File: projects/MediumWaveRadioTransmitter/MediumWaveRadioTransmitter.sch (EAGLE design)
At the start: 20 parts, among them P4 100k, Q1 400kH, T1 BC337, T2 BC337

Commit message: fix: mwrt fixed a little bit
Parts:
- removed 12V, GND, TP1, TP2, TP3: SE13, solpad:SE13
- added X1: IN_OUT, con-wago-508:W237-05P
- T1, T2: device transistor:BC337 -> transistor:BC337-16-NPN-TO92-CBE
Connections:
- removed net N$4: C1.2, C2.2, C3.2, GND.MP, P4.A, Q1.2, R8.1, R9.1
- new net GND: C1.2, C2.2, C3.2, P4.A, Q1.2, R8.1, R9.1, X1-5.KL
- net N$10: now also X1-3.KL; no longer TP2.MP
- net N$5: now also X1-2.KL; no longer TP1.MP
- net N$7: now also X1-1.KL; no longer 12V.MP
- net N$8: now also X1-4.KL; no longer TP3.MP
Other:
- moved on the sheet: C1, C2, C3, P4, R7

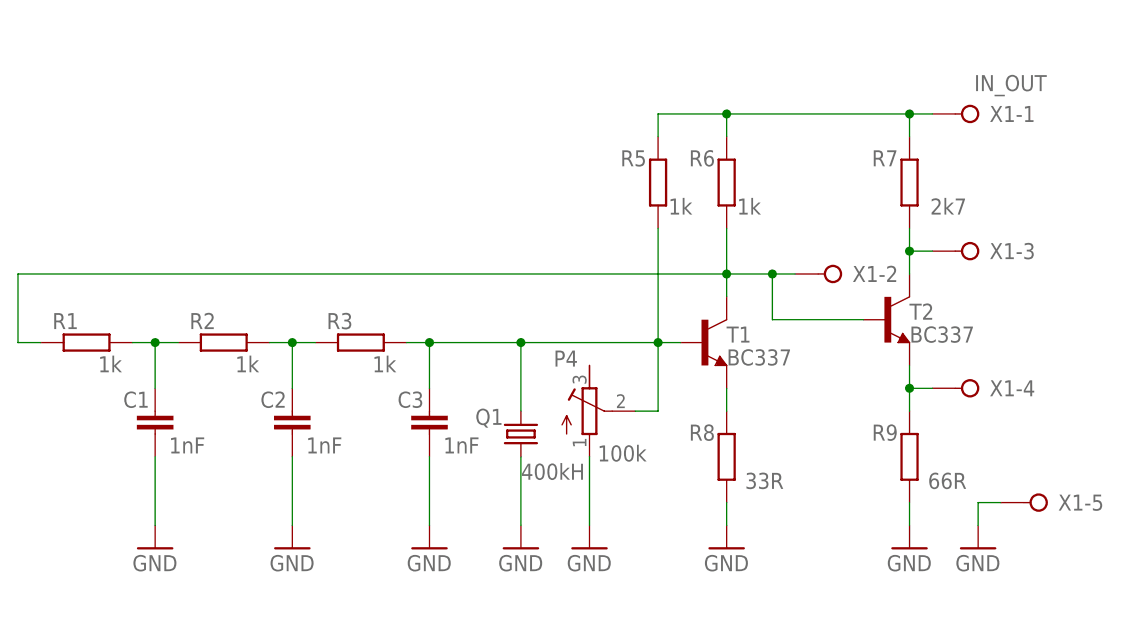
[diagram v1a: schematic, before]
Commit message: fix: medium wave radio transmitter
changes:
- schematic fixed (capacitor packages)
- routing fixed (capacitor packages)
- new gerber files added
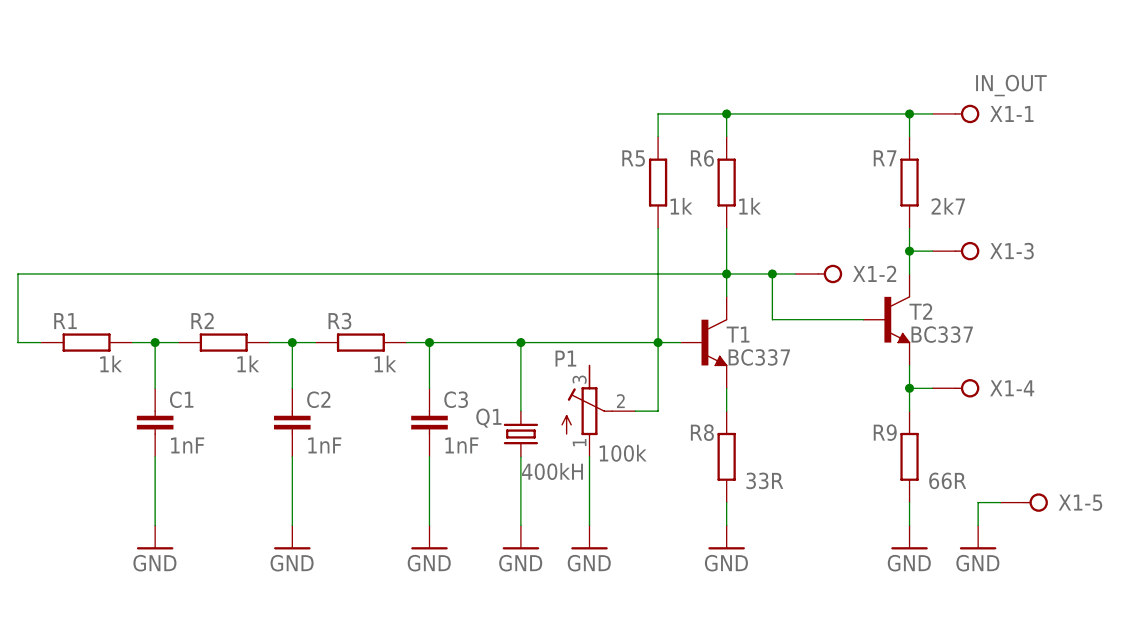
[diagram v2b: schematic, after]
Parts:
- C1, C2, C3: device capacitor-wima:C2.5/2 -> rcl:C-EU050-024X044
- renumbered P4 to P1
